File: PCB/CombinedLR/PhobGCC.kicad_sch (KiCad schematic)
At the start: 80 parts, among them J1 Conn_01x06_Female, J2 Conn_01x04_Female, J3 Conn_01x01_Male, J4 Conn_01x04_Male, J5 Conn_01x02_Male, J7 Conn_01x02_Male, Q1 Q_NMOS_GSD, Q2 Q_PMOS_GDS, Q3 Q_NMOS_GSD, SW1 A, SW10 Dup, SW11 Dright, SW12 Ddown, SW13 LB, SW14 RB, SW2 B, SW3 X, SW4 Y, SW5 Start, SW6 L, SW7 R, SW8 1825027-5, SW9 Dleft, U1 Teensy4.0, U2 2x DRV5053CAQLPGM Hall Effect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, U3 GP2S60-MFG, U4 GP2S60-MFG, U5 Stickbox_Assembly

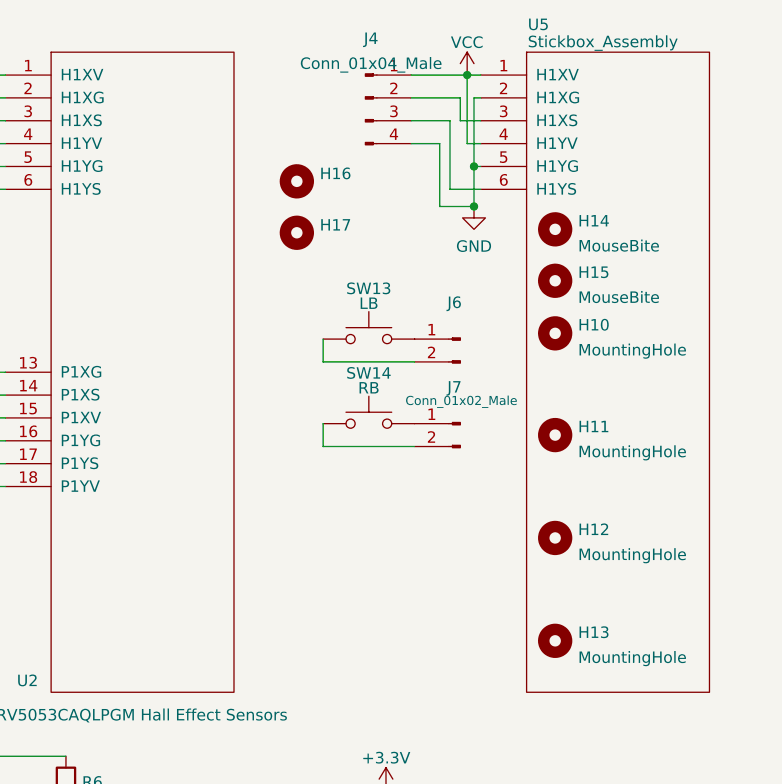
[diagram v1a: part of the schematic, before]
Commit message: fixed LR board mouse switch footprint
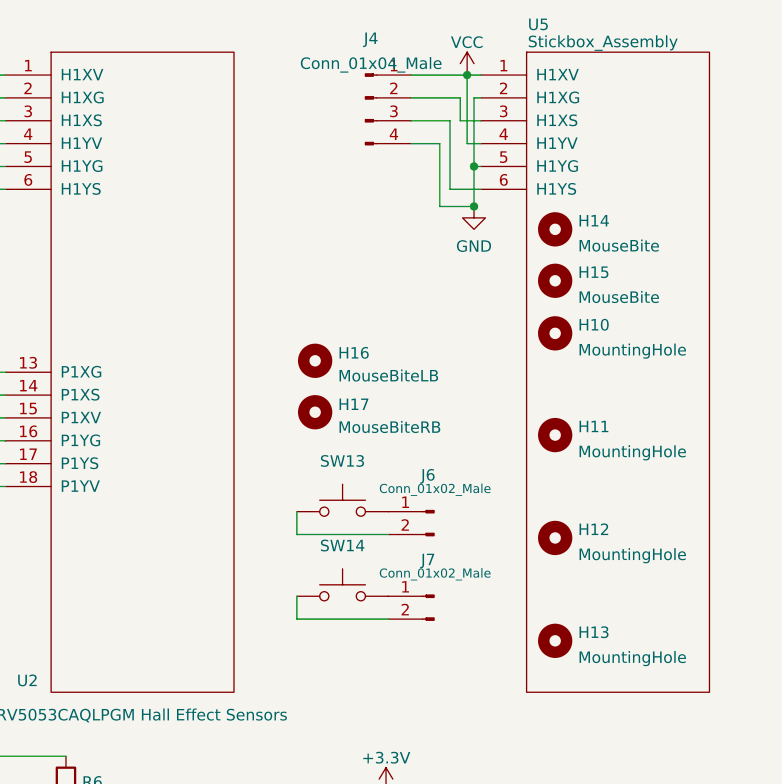
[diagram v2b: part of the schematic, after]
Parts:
- H16: value (none) -> MouseBiteLB; footprint (none) -> PhobGCC_Footprints:breakaway-mousebites
- H17: value (none) -> MouseBiteRB; footprint (none) -> PhobGCC_Footprints:breakaway-mousebites
- J6: value (none) -> Conn_01x02_Male
- SW13: value LB -> (none); footprint PhobGCC_Footprints:Trigger_Contact -> (none)
- SW14: value RB -> (none)
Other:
- moved on the sheet: H16, H17, J6, J7, SW13, SW14
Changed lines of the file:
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@@
     (stroke (width 0) (type default) (color 0 0 0 0))
   )
-  (wire (pts (xy 233.045 53.975) (xy 243.205 53.975))
+  (wire (pts (xy 230.124 73.152) (xy 240.284 73.152))
     (stroke (width 0) (type default) (color 0 0 0 0))
   )
@@
     (stroke (width 0) (type default) (color 0 0 0 0))
   )
-  (wire (pts (xy 233.045 60.833) (xy 233.045 63.373))
+  (wire (pts (xy 230.124 80.01) (xy 230.124 82.55))
     (stroke (width 0) (type default) (color 0 0 0 0))
   )
@@
     (stroke (width 0) (type default) (color 0 0 0 0))
   )
-  (wire (pts (xy 233.045 63.373) (xy 243.205 63.373))
+  (wire (pts (xy 230.124 82.55) (xy 240.284 82.55))
     (stroke (width 0) (type default) (color 0 0 0 0))
   )
@@
     (stroke (width 0) (type default) (color 0 0 0 0))
   )
-  (wire (pts (xy 233.045 51.435) (xy 233.045 53.975))
+  (wire (pts (xy 230.124 70.612) (xy 230.124 73.152))
     (stroke (width 0) (type default) (color 0 0 0 0))
   )
@@
     (pin "1")
   )
-  (symbol (lib_id "Connector:Conn_01x02_Male") (at 248.285 51.435 0) (mirror y) (unit 1)
+  (symbol (lib_id "Connector:Conn_01x02_Male") (at 245.364 70.612 0) (mirror y) (unit 1)
     (in_bom yes) (on_board yes)
-    (property "Reference" "J6" (id 0) (at 247.65 47.3923 0))
-    (property "Value" "" (id 1) (at 248.412 48.895 0)
+    (property "Reference" "J6" (id 0) (at 244.729 66.5693 0))
+    (property "Value" "Conn_01x02_Male" (id 1) (at 245.491 68.072 0)
       (effects (font (size 1 1)))
     )
-    (property "Footprint" "Connector_PinHeader_2.54mm:PinHeader_1x02_P2.54mm_Vertical" (id 2) (at 248.285 51.435 0)
+    (property "Footprint" "Connector_PinHeader_2.54mm:PinHeader_1x02_P2.54mm_Vertical" (id 2) (at 245.364 70.612 0)
       (effects (font (size 1.27 1.27)) hide)
     )
-    (property "Datasheet" "~" (id 3) (at 248.285 51.435 0)
+    (property "Datasheet" "~" (id 3) (at 245.364 70.612 0)
       (effects (font (size 1.27 1.27)) hide)
     )
@@
     (pin "2")
   )
-  (symbol (lib_id "Connector:Conn_01x02_Male") (at 248.285 60.833 0) (mirror y) (unit 1)
+  (symbol (lib_id "Connector:Conn_01x02_Male") (at 245.364 80.01 0) (mirror y) (unit 1)
     (in_bom yes) (on_board yes)
-    (property "Reference" "J7" (id 0) (at 247.65 56.7903 0))
-    (property "Value" "Conn_01x02_Male" (id 1) (at 248.412 58.293 0)
+    (property "Reference" "J7" (id 0) (at 244.729 75.9673 0))
+    (property "Value" "Conn_01x02_Male" (id 1) (at 245.491 77.47 0)
       (effects (font (size 1 1)))
     )
-    (property "Footprint" "Connector_PinHeader_2.54mm:PinHeader_1x02_P2.54mm_Vertical" (id 2) (at 248.285 60.833 0)
+    (property "Footprint" "Connector_PinHeader_2.54mm:PinHeader_1x02_P2.54mm_Vertical" (id 2) (at 245.364 80.01 0)
       (effects (font (size 1.27 1.27)) hide)
     )
-    (property "Datasheet" "~" (id 3) (at 248.285 60.833 0)
+    (property "Datasheet" "~" (id 3) (at 245.364 80.01 0)
       (effects (font (size 1.27 1.27)) hide)
     )
@@
     (pin "4")
   )
-  (symbol (lib_id "Mechanical:MountingHole") (at 230.124 33.909 0) (unit 1)
+  (symbol (lib_id "Mechanical:MountingHole") (at 232.156 53.848 0) (unit 1)
     (in_bom yes) (on_board yes) (fields_autoplaced)
-    (property "Reference" "H16" (id 0) (at 232.664 33.0743 0)
+    (property "Reference" "H16" (id 0) (at 234.696 53.0133 0)
       (effects (font (size 1.27 1.27)) (justify left))
     )
-    (property "Value" "" (id 1) (at 232.664 35.6112 0)
+    (property "Value" "MouseBiteLB" (id 1) (at 234.696 55.5502 0)
       (effects (font (size 1.27 1.27)) (justify left))
     )
-    (property "Footprint" "" (id 2) (at 230.124 33.909 0)
+    (property "Footprint" "PhobGCC_Footprints:breakaway-mousebites" (id 2) (at 232.156 53.848 0)
       (effects (font (size 1.27 1.27)) hide)
     )
-    (property "Datasheet" "~" (id 3) (at 230.124 33.909 0)
+    (property "Datasheet" "~" (id 3) (at 232.156 53.848 0)
       (effects (font (size 1.27 1.27)) hide)
     )
@@
     )
   )
-  (symbol (lib_name "SW_Push_2") (lib_id "Switch:SW_Push") (at 238.125 60.833 0) (unit 1)
+  (symbol (lib_name "SW_Push_2") (lib_id "Switch:SW_Push") (at 235.204 80.01 0) (unit 1)
     (in_bom yes) (on_board yes)
-    (property "Reference" "SW14" (id 0) (at 238.125 55.245 0))
-    (property "Value" "RB" (id 1) (at 238.125 56.896 0))
-    (property "Footprint" "PhobGCC_Footprints:Trigger_Contact" (id 2) (at 238.125 55.753 0)
+    (property "Reference" "SW14" (id 0) (at 235.204 74.422 0))
+    (property "Value" "" (id 1) (at 235.204 76.073 0))
+    (property "Footprint" "PhobGCC_Footprints:Trigger_Contact" (id 2) (at 235.204 74.93 0)
       (effects (font (size 1.27 1.27)) hide)
     )
-    (property "Datasheet" "~" (id 3) (at 238.125 55.753 0)
+    (property "Datasheet" "~" (id 3) (at 235.204 74.93 0)
       (effects (font (size 1.27 1.27)) hide)
     )
@@
     (pin "2")
   )
-  (symbol (lib_id "Mechanical:MountingHole") (at 230.124 39.624 0) (unit 1)
+  (symbol (lib_id "Mechanical:MountingHole") (at 232.156 59.563 0) (unit 1)
     (in_bom yes) (on_board yes) (fields_autoplaced)
-    (property "Reference" "H17" (id 0) (at 232.664 38.7893 0)
+    (property "Reference" "H17" (id 0) (at 234.696 58.7283 0)
       (effects (font (size 1.27 1.27)) (justify left))
     )
-    (property "Value" "" (id 1) (at 232.664 41.3262 0)
+    (property "Value" "MouseBiteRB" (id 1) (at 234.696 61.2652 0)
       (effects (font (size 1.27 1.27)) (justify left))
     )
-    (property "Footprint" "" (id 2) (at 230.124 39.624 0)
+    (property "Footprint" "PhobGCC_Footprints:breakaway-mousebites" (id 2) (at 232.156 59.563 0)
       (effects (font (size 1.27 1.27)) hide)
     )
-    (property "Datasheet" "~" (id 3) (at 230.124 39.624 0)
+    (property "Datasheet" "~" (id 3) (at 232.156 59.563 0)
       (effects (font (size 1.27 1.27)) hide)
     )
@@
     (pin "1")
   )
-  (symbol (lib_name "SW_Push_1") (lib_id "Switch:SW_Push") (at 238.125 51.435 0) (unit 1)
+  (symbol (lib_name "SW_Push_1") (lib_id "Switch:SW_Push") (at 235.204 70.612 0) (unit 1)
     (in_bom yes) (on_board yes)
-    (property "Reference" "SW13" (id 0) (at 238.125 45.847 0))
-    (property "Value" "LB" (id 1) (at 238.125 47.498 0))
-    (property "Footprint" "PhobGCC_Footprints:Trigger_Contact" (id 2) (at 238.125 46.355 0)
+    (property "Reference" "SW13" (id 0) (at 235.204 65.024 0))
+    (property "Value" "" (id 1) (at 235.204 66.675 0))
+    (property "Footprint" "" (id 2) (at 235.204 65.532 0)
       (effects (font (size 1.27 1.27)) hide)
     )
-    (property "Datasheet" "~" (id 3) (at 238.125 46.355 0)
+    (property "Datasheet" "~" (id 3) (at 235.204 65.532 0)
       (effects (font (size 1.27 1.27)) hide)
     )
@@
     )
     (path "/ecab30c4-546c-46da-8332-d218e09ac3ff"
-      (reference "SW13") (unit 1) (value "LB") (footprint "PhobGCC_Footprints:Trigger_Contact")
+      (reference "SW13") (unit 1) (value "L") (footprint "PhobGCC_Footprints:Trigger_Contact")
     )
     (path "/da06455a-cfd6-4278-a2c0-9c38c8567165"
-      (reference "SW14") (unit 1) (value "RB") (footprint "PhobGCC_Footprints:Trigger_Contact")
+      (reference "SW14") (unit 1) (value "R") (footprint "PhobGCC_Footprints:Trigger_Contact")
     )
     (path "/00000000-0000-0000-0000-00006154c933"

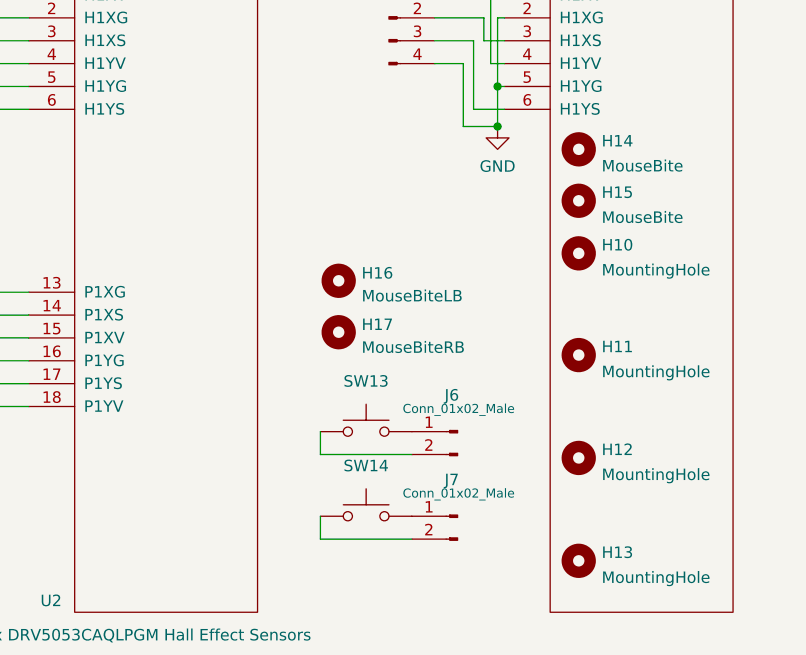
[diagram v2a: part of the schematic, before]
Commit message: flipped trigger boards
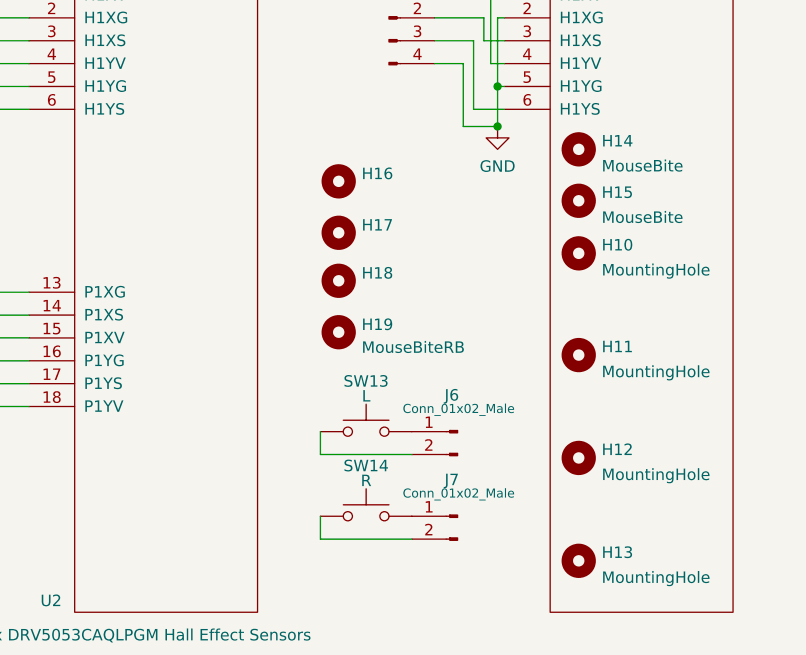
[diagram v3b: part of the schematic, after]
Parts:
- added H16, H17: (no value), PhobGCC_Footprints:breakaway-mousebites, symbol Mechanical:MountingHole
- H18: renamed from H16; value MouseBiteLB -> (none)
- SW13: value (none) -> L; footprint (none) -> PhobGCC_Footprints:Trigger_Contact
- SW14: value (none) -> R
- renumbered H17 to H19
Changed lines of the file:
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@@
     (pin "2")
+  )
+  (symbol (lib_id "Mechanical:MountingHole") (at 232.156 42.799 0) (unit 1)
+    (in_bom yes) (on_board yes) (fields_autoplaced)
+    (property "Reference" "H16" (id 0) (at 234.696 41.9643 0)
+      (effects (font (size 1.27 1.27)) (justify left))
+    )
+    (property "Value" "" (id 1) (at 234.696 44.5012 0)
+      (effects (font (size 1.27 1.27)) (justify left))
+    )
+    (property "Footprint" "PhobGCC_Footprints:breakaway-mousebites" (id 2) (at 232.156 42.799 0)
+      (effects (font (size 1.27 1.27)) hide)
+    )
+    (property "Datasheet" "~" (id 3) (at 232.156 42.799 0)
+      (effects (font (size 1.27 1.27)) hide)
+    )
   )
   (symbol (lib_id "Mechanical:MountingHole") (at 258.826 50.8 0) (unit 1)
@@
   (symbol (lib_id "Mechanical:MountingHole") (at 232.156 53.848 0) (unit 1)
     (in_bom yes) (on_board yes) (fields_autoplaced)
-    (property "Reference" "H16" (id 0) (at 234.696 53.0133 0)
-      (effects (font (size 1.27 1.27)) (justify left))
-    )
-    (property "Value" "MouseBiteLB" (id 1) (at 234.696 55.5502 0)
+    (property "Reference" "H18" (id 0) (at 234.696 53.0133 0)
+      (effects (font (size 1.27 1.27)) (justify left))
+    )
+    (property "Value" "" (id 1) (at 234.696 55.5502 0)
       (effects (font (size 1.27 1.27)) (justify left))
     )
@@
     (in_bom yes) (on_board yes)
     (property "Reference" "SW14" (id 0) (at 235.204 74.422 0))
-    (property "Value" "" (id 1) (at 235.204 76.073 0))
+    (property "Value" "R" (id 1) (at 235.204 76.073 0))
     (property "Footprint" "PhobGCC_Footprints:Trigger_Contact" (id 2) (at 235.204 74.93 0)
       (effects (font (size 1.27 1.27)) hide)
@@
   (symbol (lib_id "Mechanical:MountingHole") (at 232.156 59.563 0) (unit 1)
     (in_bom yes) (on_board yes) (fields_autoplaced)
-    (property "Reference" "H17" (id 0) (at 234.696 58.7283 0)
+    (property "Reference" "H19" (id 0) (at 234.696 58.7283 0)
       (effects (font (size 1.27 1.27)) (justify left))
     )
@@
     (in_bom yes) (on_board yes)
     (property "Reference" "SW13" (id 0) (at 235.204 65.024 0))
-    (property "Value" "" (id 1) (at 235.204 66.675 0))
-    (property "Footprint" "" (id 2) (at 235.204 65.532 0)
+    (property "Value" "L" (id 1) (at 235.204 66.675 0))
+    (property "Footprint" "PhobGCC_Footprints:Trigger_Contact" (id 2) (at 235.204 65.532 0)
       (effects (font (size 1.27 1.27)) hide)
     )
@@
     (pin "1")
     (pin "2")
+  )
+  (symbol (lib_id "Mechanical:MountingHole") (at 232.156 48.514 0) (unit 1)
+    (in_bom yes) (on_board yes) (fields_autoplaced)
+    (property "Reference" "H17" (id 0) (at 234.696 47.6793 0)
+      (effects (font (size 1.27 1.27)) (justify left))
+    )
+    (property "Value" "" (id 1) (at 234.696 50.2162 0)
+      (effects (font (size 1.27 1.27)) (justify left))
+    )
+    (property "Footprint" "PhobGCC_Footprints:breakaway-mousebites" (id 2) (at 232.156 48.514 0)
+      (effects (font (size 1.27 1.27)) hide)
+    )
+    (property "Datasheet" "~" (id 3) (at 232.156 48.514 0)
+      (effects (font (size 1.27 1.27)) hide)
+    )
   )
   (symbol (lib_id "Device:C") (at 118.11 119.38 0) (unit 1)
@@
       (reference "H15") (unit 1) (value "MouseBite") (footprint "PhobGCC_Footprints:mouse-bite-2.54mm-slot")
     )
+    (path "/230dbd27-c408-46e6-9710-e9e10e77e86a"
+      (reference "H16") (unit 1) (value "MouseBiteLA") (footprint "PhobGCC_Footprints:breakaway-mousebites")
+    )
+    (path "/eda2a986-16a5-4022-b1d6-2552e61abdd1"
+      (reference "H17") (unit 1) (value "MouseBiteLB") (footprint "PhobGCC_Footprints:breakaway-mousebites")
+    )
     (path "/cee780b2-d029-4e98-8379-2557c9e148e3"
-      (reference "H16") (unit 1) (value "MouseBiteLB") (footprint "PhobGCC_Footprints:breakaway-mousebites")
+      (reference "H18") (unit 1) (value "MouseBiteRA") (footprint "PhobGCC_Footprints:breakaway-mousebites")
     )
     (path "/df2bc5b1-8420-4d9c-936b-e42e3b416681"
-      (reference "H17") (unit 1) (value "MouseBiteRB") (footprint "PhobGCC_Footprints:breakaway-mousebites")
+      (reference "H19") (unit 1) (value "MouseBiteRB") (footprint "PhobGCC_Footprints:breakaway-mousebites")
     )
     (path "/00000000-0000-0000-0000-000061572882"
